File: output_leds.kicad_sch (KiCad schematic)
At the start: 43 parts, among them U601 74HC595, U602 74HC595

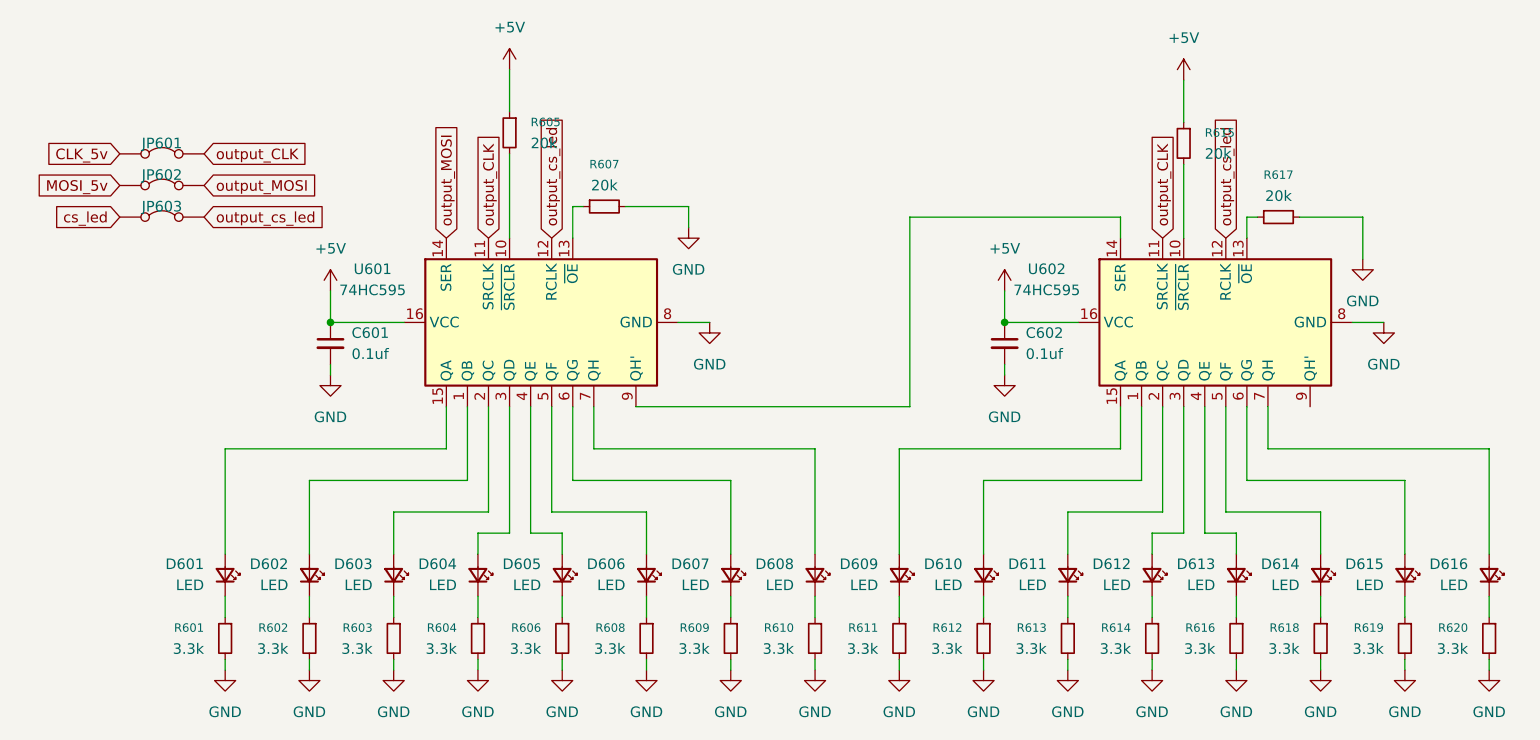
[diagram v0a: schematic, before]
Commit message: schematic done, routed dac ladder
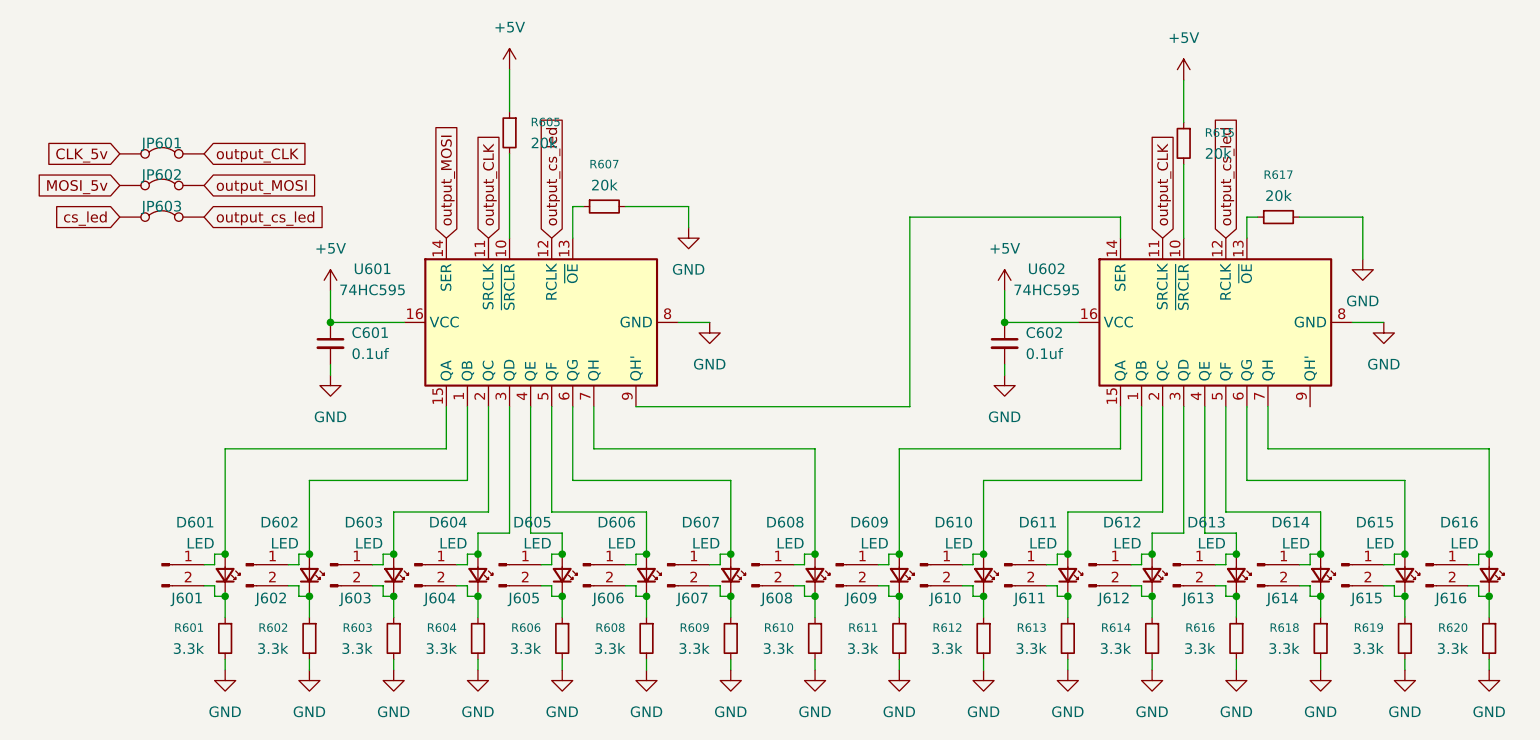
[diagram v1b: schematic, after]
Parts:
- added J601, J602, J603, J604, J605, J606, J607, J608, J609, J610, J611, J612, J613, J614, J615, J616: Conn_01x02_Pin, Connector_PinSocket_2.54mm:PinSocket_1x02_P2.54mm_Vertical, symbol Connector:Conn_01x02_Pin
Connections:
- net at D608.1 (K), R610.1: now also J608.2 (Pin_2)
- net at D616.1 (K), R620.1: now also J616.2 (Pin_2)
- net at D616.2 (A), U602.7 (QH): now also J616.1 (Pin_1)
- net at D611.1 (K), R613.1: now also J611.2 (Pin_2)
- net at D611.2 (A), U602.2 (QC): now also J611.1 (Pin_1)
- net at D605.1 (K), R606.1: now also J605.2 (Pin_2)
- net at D613.1 (K), R616.1: now also J613.2 (Pin_2)
- net at D613.2 (A), U602.4 (QE): now also J613.1 (Pin_1)
- net at D612.1 (K), R614.1: now also J612.2 (Pin_2)
- net at D601.1 (K), R601.1: now also J601.2 (Pin_2)
- net at D601.2 (A), U601.15 (QA): now also J601.1 (Pin_1)
- net at D603.1 (K), R603.1: now also J603.2 (Pin_2)
- net at D606.1 (K), R608.1: now also J606.2 (Pin_2)
- net at D606.2 (A), U601.5 (QF): now also J606.1 (Pin_1)
- net at D614.1 (K), R618.1: now also J614.2 (Pin_2)
- net at D614.2 (A), U602.5 (QF): now also J614.1 (Pin_1)
- net at D610.1 (K), R612.1: now also J610.2 (Pin_2)
- net at D610.2 (A), U602.1 (QB): now also J610.1 (Pin_1)
- net at D609.2 (A), U602.15 (QA): now also J609.1 (Pin_1)
- net at D612.2 (A), U602.3 (QD): now also J612.1 (Pin_1)
- net at D615.2 (A), U602.6 (QG): now also J615.1 (Pin_1)
- net at D604.1 (K), R604.1: now also J604.2 (Pin_2)
- net at D605.2 (A), U601.4 (QE): now also J605.1 (Pin_1)
- net at D609.1 (K), R611.1: now also J609.2 (Pin_2)
- net at D602.2 (A), U601.1 (QB): now also J602.1 (Pin_1)
- net at D603.2 (A), U601.2 (QC): now also J603.1 (Pin_1)
- net at D604.2 (A), U601.3 (QD): now also J604.1 (Pin_1)
- net at D607.2 (A), U601.6 (QG): now also J607.1 (Pin_1)
- net at D608.2 (A), U601.7 (QH): now also J608.1 (Pin_1)
- net at D602.1 (K), R602.1: now also J602.2 (Pin_2)
- net at D607.1 (K), R609.1: now also J607.2 (Pin_2)
- net at D615.1 (K), R619.1: now also J615.2 (Pin_2)

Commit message: grouped components in board
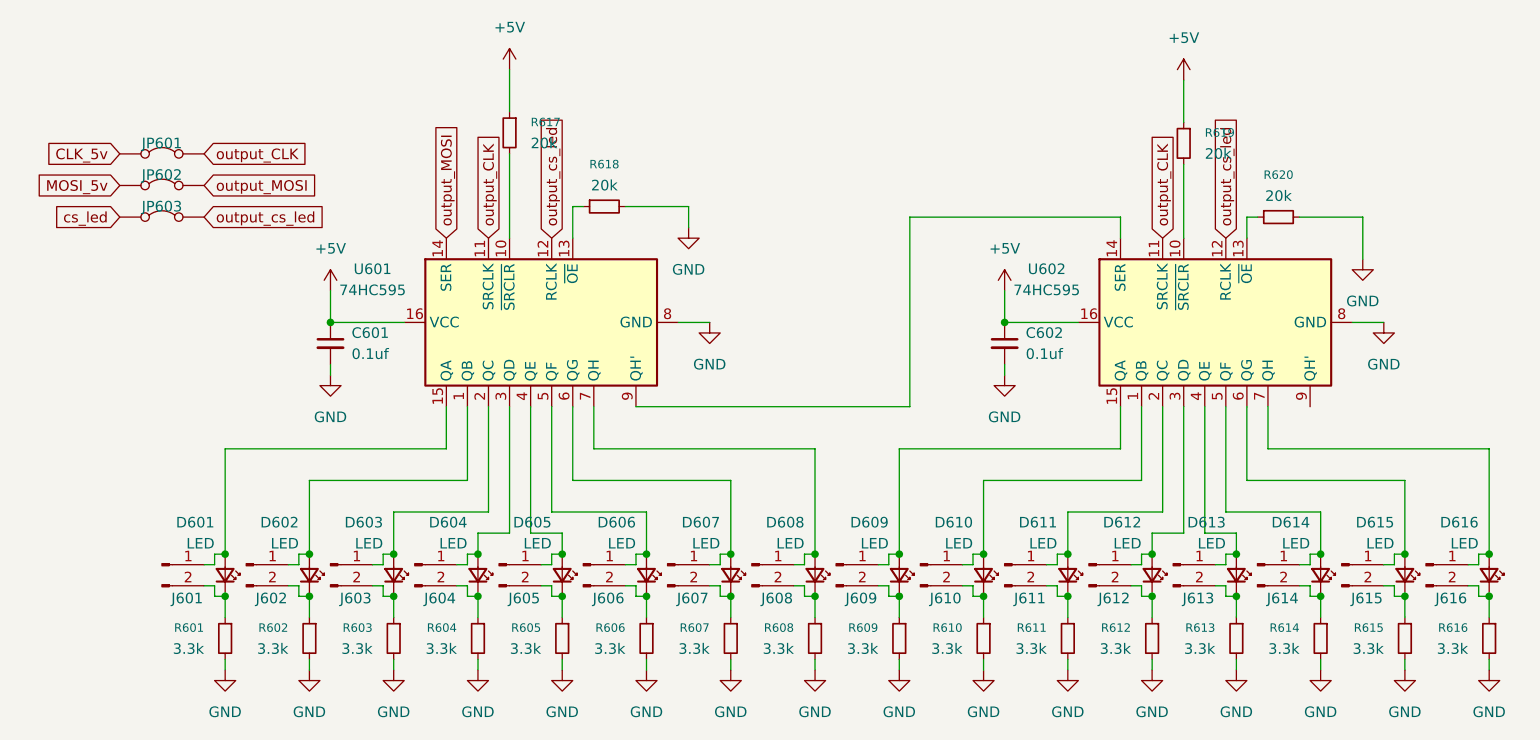
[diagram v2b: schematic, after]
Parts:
- renumbered R606 to R605, R608 to R606, R609 to R607, R610 to R608, R611 to R609, R612 to R610, R613 to R611, R614 to R612, R616 to R613, R618 to R614, R619 to R615, R620 to R616, R605 to R617, R607 to R618, R615 to R619, R617 to R620
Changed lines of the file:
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@@
 		(dnp no)
 		(fields_autoplaced yes)
-		(property "Reference" "R610"
+		(property "Reference" "R608"
 			(at 123.19 92.7099 0)
 			(effects
@@
 			(project "nano_sequencer"
 				(path "/335d65e6-88b4-479c-8bfd-74e13066bd23/ef302e78-da1b-4a46-affc-92636b526e4a"
-					(reference "R610")
+					(reference "R608")
 					(unit 1)
 				)
@@
 		(dnp no)
 		(fields_autoplaced yes)
-		(property "Reference" "R606"
+		(property "Reference" "R605"
 			(at 92.71 92.7099 0)
 			(effects
@@
 			(project "nano_sequencer"
 				(path "/335d65e6-88b4-479c-8bfd-74e13066bd23/ef302e78-da1b-4a46-affc-92636b526e4a"
-					(reference "R606")
+					(reference "R605")
 					(unit 1)
 				)
@@
 		(dnp no)
 		(fields_autoplaced yes)
-		(property "Reference" "R614"
+		(property "Reference" "R612"
 			(at 163.83 92.7099 0)
 			(effects
@@
 			(project "nano_sequencer"
 				(path "/335d65e6-88b4-479c-8bfd-74e13066bd23/ef302e78-da1b-4a46-affc-92636b526e4a"
-					(reference "R614")
+					(reference "R612")
 					(unit 1)
 				)
@@
 		(dnp no)
 		(fields_autoplaced yes)
-		(property "Reference" "R615"
+		(property "Reference" "R619"
 			(at 172.72 33.0199 0)
 			(effects
@@
 			(project "nano_sequencer"
 				(path "/335d65e6-88b4-479c-8bfd-74e13066bd23/ef302e78-da1b-4a46-affc-92636b526e4a"
-					(reference "R615")
+					(reference "R619")
 					(unit 1)
 				)
@@
 		(dnp no)
 		(fields_autoplaced yes)
-		(property "Reference" "R605"
+		(property "Reference" "R617"
 			(at 91.44 31.7499 0)
 			(effects
@@
 			(project "nano_sequencer"
 				(path "/335d65e6-88b4-479c-8bfd-74e13066bd23/ef302e78-da1b-4a46-affc-92636b526e4a"
-					(reference "R605")
+					(reference "R617")
 					(unit 1)
 				)
@@
 		(dnp no)
 		(fields_autoplaced yes)
-		(property "Reference" "R613"
+		(property "Reference" "R611"
 			(at 153.67 92.7099 0)
 			(effects
@@
 			(project "nano_sequencer"
 				(path "/335d65e6-88b4-479c-8bfd-74e13066bd23/ef302e78-da1b-4a46-affc-92636b526e4a"
-					(reference "R613")
+					(reference "R611")
 					(unit 1)
 				)
@@
 		(dnp no)
 		(fields_autoplaced yes)
-		(property "Reference" "R616"
+		(property "Reference" "R613"
 			(at 173.99 92.7099 0)
 			(effects
@@
 			(project "nano_sequencer"
 				(path "/335d65e6-88b4-479c-8bfd-74e13066bd23/ef302e78-da1b-4a46-affc-92636b526e4a"
-					(reference "R616")
+					(reference "R613")
 					(unit 1)
 				)
@@
 		(dnp no)
 		(fields_autoplaced yes)
-		(property "Reference" "R608"
+		(property "Reference" "R606"
 			(at 102.87 92.7099 0)
 			(effects
@@
 			(project "nano_sequencer"
 				(path "/335d65e6-88b4-479c-8bfd-74e13066bd23/ef302e78-da1b-4a46-affc-92636b526e4a"
-					(reference "R608")
+					(reference "R606")
 					(unit 1)
 				)
@@
 		(dnp no)
 		(fields_autoplaced yes)
-		(property "Reference" "R611"
+		(property "Reference" "R609"
 			(at 133.35 92.7099 0)
 			(effects
@@
 			(project "nano_sequencer"
 				(path "/335d65e6-88b4-479c-8bfd-74e13066bd23/ef302e78-da1b-4a46-affc-92636b526e4a"
-					(reference "R611")
+					(reference "R609")
 					(unit 1)
 				)
@@
 		(dnp no)
 		(fields_autoplaced yes)
-		(property "Reference" "R612"
+		(property "Reference" "R610"
 			(at 143.51 92.7099 0)
 			(effects
@@
 			(project "nano_sequencer"
 				(path "/335d65e6-88b4-479c-8bfd-74e13066bd23/ef302e78-da1b-4a46-affc-92636b526e4a"
-					(reference "R612")
+					(reference "R610")
 					(unit 1)
 				)
@@
 		(dnp no)
 		(fields_autoplaced yes)
-		(property "Reference" "R607"
+		(property "Reference" "R618"
 			(at 100.33 36.83 90)
 			(effects
@@
 			(project "nano_sequencer"
 				(path "/335d65e6-88b4-479c-8bfd-74e13066bd23/ef302e78-da1b-4a46-affc-92636b526e4a"
-					(reference "R607")
+					(reference "R618")
 					(unit 1)
 				)
@@
 		(dnp no)
 		(fields_autoplaced yes)
-		(property "Reference" "R620"
+		(property "Reference" "R616"
 			(at 204.47 92.7099 0)
 			(effects
@@
 			(project "nano_sequencer"
 				(path "/335d65e6-88b4-479c-8bfd-74e13066bd23/ef302e78-da1b-4a46-affc-92636b526e4a"
-					(reference "R620")
+					(reference "R616")
 					(unit 1)
 				)
@@
 		(dnp no)
 		(fields_autoplaced yes)
-		(property "Reference" "R609"
+		(property "Reference" "R607"
 			(at 113.03 92.7099 0)
 			(effects
@@
 			(project "nano_sequencer"
 				(path "/335d65e6-88b4-479c-8bfd-74e13066bd23/ef302e78-da1b-4a46-affc-92636b526e4a"
-					(reference "R609")
+					(reference "R607")
 					(unit 1)
 				)
@@
 		(dnp no)
 		(fields_autoplaced yes)
-		(property "Reference" "R618"
+		(property "Reference" "R614"
 			(at 184.15 92.7099 0)
 			(effects
@@
 			(project "nano_sequencer"
 				(path "/335d65e6-88b4-479c-8bfd-74e13066bd23/ef302e78-da1b-4a46-affc-92636b526e4a"
-					(reference "R618")
+					(reference "R614")
 					(unit 1)
 				)
@@
 		(on_board yes)
 		(dnp no)
-		(fields_autoplaced yes)
 		(property "Reference" "#PWR0603"
 			(at 67.31 55.88 0)
@@
 		(dnp no)
 		(fields_autoplaced yes)
-		(property "Reference" "R619"
+		(property "Reference" "R615"
 			(at 194.31 92.7099 0)
 			(effects
@@
 			(project "nano_sequencer"
 				(path "/335d65e6-88b4-479c-8bfd-74e13066bd23/ef302e78-da1b-4a46-affc-92636b526e4a"
-					(reference "R619")
+					(reference "R615")
 					(unit 1)
 				)
@@
 		(dnp no)
 		(fields_autoplaced yes)
-		(property "Reference" "R617"
+		(property "Reference" "R620"
 			(at 181.61 38.1 90)
 			(effects
@@
 			(project "nano_sequencer"
 				(path "/335d65e6-88b4-479c-8bfd-74e13066bd23/ef302e78-da1b-4a46-affc-92636b526e4a"
-					(reference "R617")
+					(reference "R620")
 					(unit 1)
 				)

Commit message: added lcsc part numbers and fabrication files
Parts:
- C601, C602: footprint LED_SMD:LED_0805_2012Metric_Pad1.15x1.40mm_HandSolder -> Capacitor_SMD:C_0805_2012Metric_Pad1.18x1.45mm_HandSolder; LCSC PN (none) -> C49678
- D601, D602, D603, D604, D605, D606, D607, D608, D609, D610, D611, D612, D613, D614, D615, D616: LCSC PN (none) -> C2297
- R601, R602, R603, R604, R605, R606, R607, R608, R609, R610, R611, R612, R613, R614, R615, R616: value 3.3k -> 2k; LCSC PN (none) -> C17604
- R617, R618, R619, R620: LCSC PN (none) -> C4328
- U601, U602: LCSC PN (none) -> C5947
